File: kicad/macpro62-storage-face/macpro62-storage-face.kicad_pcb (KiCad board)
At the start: 6 copper layers, 104 x 166 mm, 73 parts, among them J1 J_PCIE MCIO124 RA G97R24332HR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, J20 BUSBAR LUG site A +12V_IN (po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, J21 BUSBAR LUG site A GND (polari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, J22 BUSBAR LUG site B +12V_IN (po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, J23 BUSBAR LUG site B GND (polari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, J3 J_AUX GH15 RA SM15B-GHS-TB (m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, J5 M.2 M-key H4.2 SSD0 (LOTES AP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, J6 M.2 M-key H4.2 SSD1 (LOTES AP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, J7 M.2 M-key H4.2 SSD2 (LOTES AP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, J8 M.2 M-key H4.2 SSD3 (LOTES AP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, Q1 N-MOSFET 30 V <=5 mOhm (rever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, U1 ASM2824 PCIe Gen3 switch (JLC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, U10 74LVC2G07 PERST# fan-out SSD2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, U11 TMP1075DSGR @0x49 THERM_TRIP#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, U12 74LVC2G07 switch PERST# gate 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, U2 TPS259824ONRGER eFuse I_LIM 5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, U3 LM74700-Q1 ideal-diode ctrl, U4 TPS56C215RNNR 3V3_SSD 12 A bu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, U5 TLV62585 VDD_CORE buck (rail 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, U6 BL24C64A-SFRC ID EEPROM @0x50, U7 TMP1075DSGR @0x48, U8 SPI flash 25Q (switch config,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, U9 74LVC2G07 PERST# fan-out SSD0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, Y1 25 MHz (populate only if ASM2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

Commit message: ICD rev 2: 45 deg faces, 445 W ceiling + live power target (INA228 telemetry), ribbon MCIO jog cables, BT on S0, fan fail-safe, port-module I2C map
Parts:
- added C520: 100nF U13 VS, MP62_Storage:C_0402_1005Metric, B.Cu at (111.5, 49.5)
- added R520: 2 mOhm 2512 shunt (+12V_PROT -> U2), MP62_Storage:R_2512_6332Metric, B.Cu at (104.0, 47.0)
- added U13: INA228 @0x40 FACE_SMB, ALERT -> FACE_SMB_ALERT#, MP62_Storage:VSSOP-10_3x3mm_P0.5mm, B.Cu at (111.5, 47.0)

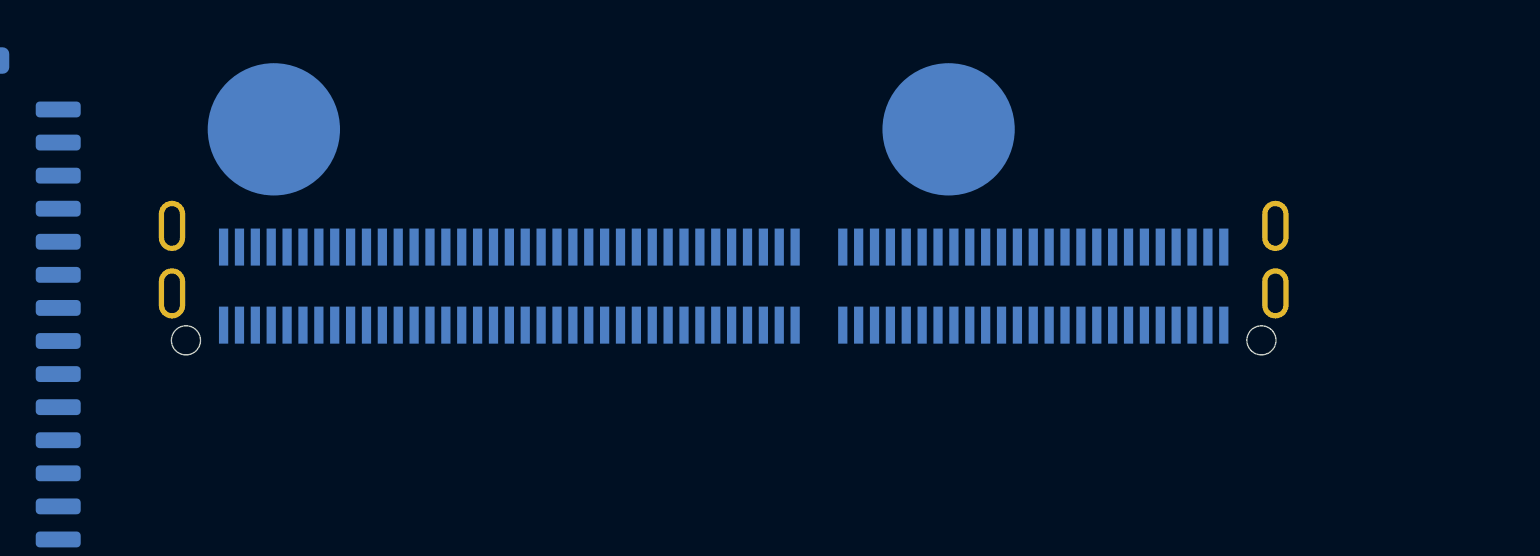
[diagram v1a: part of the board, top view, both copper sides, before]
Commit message: O-10: zero-jog MCIO (face J_PCIE X47.0, J_DISP X82.5, narrow plugs), backplane fp6 re-pack, ICD rev 3
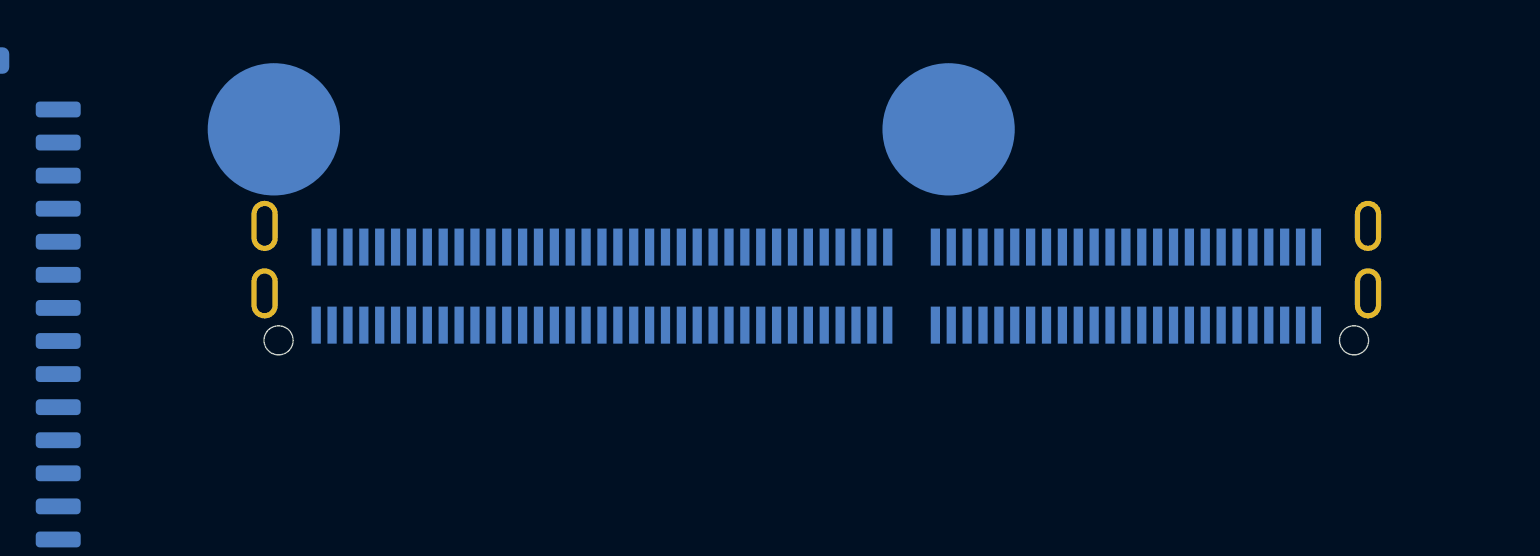
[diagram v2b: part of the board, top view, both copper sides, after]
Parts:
- moved J1 3.50 mm to (107.0, 169.5)
